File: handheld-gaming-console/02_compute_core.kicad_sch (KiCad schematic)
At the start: 33 parts, among them J3 CM4_MAIN, J4 CM4_PERIPH, J8 Micro_SD_Card, Q3 Q_PMOS_GSD, Q4 Q_NMOS_GSD, SW1 SW_SPDT, SW2 SW_Push, U5 TS3USB221A

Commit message: feat(display): implement AP3031 38V constant-current WLED backlight boost driver with PWM dimming and aux header
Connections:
- net LCD_BL_PWM: now reaches J3.54 (Pin_54)
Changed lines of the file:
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@@
+	(wire
+		(pts
+			(xy 87.63 104.14) (xy 88.9 104.14)
+		)
+		(stroke
+			(width 0)
+			(type default)
+		)
+	)
 	(wire
 		(pts
@@
 			)
 		)
+	)
+	(global_label "LCD_BL_PWM"
+		(shape input)
+		(at 88.9 104.14 0)
+		(fields_autoplaced yes)
+		(effects
+			(font
+				(size 1.27 1.27)
+			)
+			(justify left)
+		)
+		(property "Intersheetrefs" "${INTERSHEET_REFS}"
+			(at 103.8594 104.14 0)
+			(hide yes)
+			(show_name no)
+			(do_not_autoplace no)
+			(effects
+				(font
+					(size 1.27 1.27)
+				)
+				(justify left)
+			)
+		)

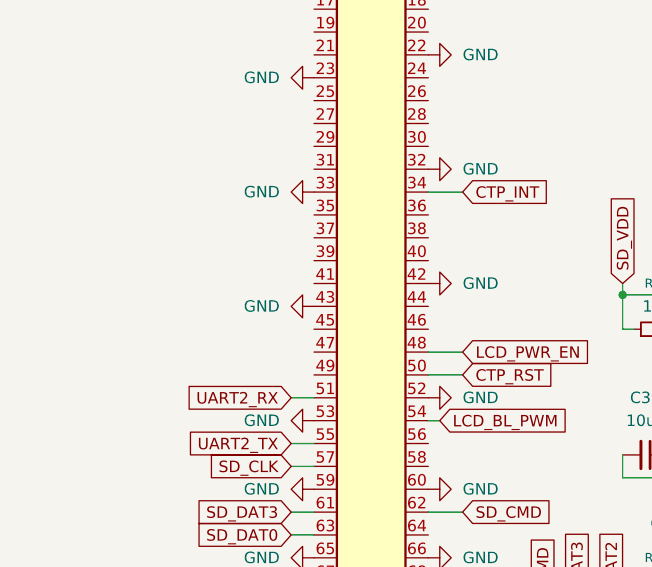
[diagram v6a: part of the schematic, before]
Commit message: feat(audio): tap I2S bus from Core3566 and implement isolated MAX98357A Class-D speaker amplifier
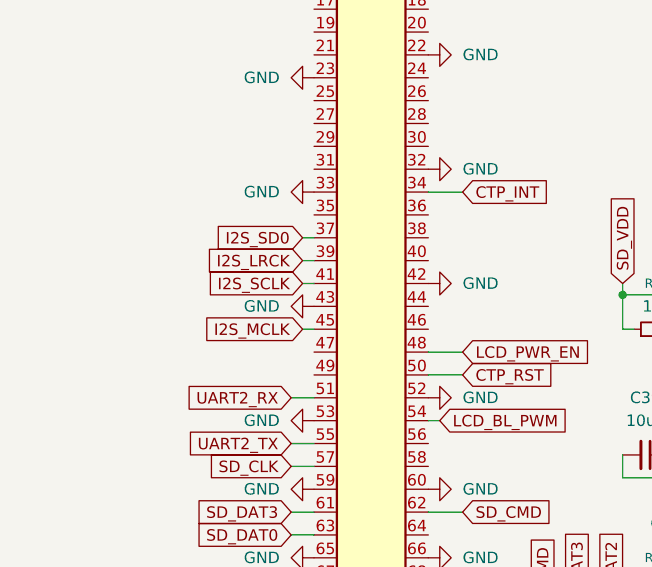
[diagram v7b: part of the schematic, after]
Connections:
- net I2S_SD0: now reaches J3.37 (Pin_37)
- net I2S_LRCK: now reaches J3.39 (Pin_39)
- net I2S_SCLK: now reaches J3.41 (Pin_41)
- net I2S_MCLK: now reaches J3.45 (Pin_45)
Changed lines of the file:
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@@
+	(wire
+		(pts
+			(xy 73.66 86.36) (xy 74.93 86.36)
+		)
+		(stroke
+			(width 0)
+			(type default)
+		)
+	)
 	(wire
 		(pts
@@
 	(wire
 		(pts
+			(xy 73.66 83.82) (xy 74.93 83.82)
+		)
+		(stroke
+			(width 0)
+			(type default)
+		)
+	)
+	(wire
+		(pts
 			(xy 223.52 55.88) (xy 251.46 55.88)
 		)
@@
 	(wire
 		(pts
+			(xy 73.66 93.98) (xy 74.93 93.98)
+		)
+		(stroke
+			(width 0)
+			(type default)
+		)
+	)
+	(wire
+		(pts
 			(xy 120.65 90.17) (xy 118.11 90.17)
 		)
@@
 	(wire
 		(pts
+			(xy 73.66 88.9) (xy 74.93 88.9)
+		)
+		(stroke
+			(width 0)
+			(type default)
+		)
+	)
+	(wire
+		(pts
 			(xy 125.73 119.38) (xy 125.73 107.95)
 		)
@@
 		)
 	)
+	(global_label "I2S_SD0"
+		(shape input)
+		(at 73.66 83.82 180)
+		(fields_autoplaced yes)
+		(effects
+			(font
+				(size 1.27 1.27)
+			)
+			(justify right)
+		)
+		(property "Intersheetrefs" "${INTERSHEET_REFS}"
+			(at 62.9944 83.82 0)
+			(hide yes)
+			(show_name no)
+			(do_not_autoplace no)
+			(effects
+				(font
+					(size 1.27 1.27)
+				)
+				(justify right)
+			)
+		)
+	)
 	(global_label "USB_OTG_ID"
 		(shape input)
@@
 		)
 	)
+	(global_label "I2S_SCLK"
+		(shape input)
+		(at 73.66 88.9 180)
+		(fields_autoplaced yes)
+		(effects
+			(font
+				(size 1.27 1.27)
+			)
+			(justify right)
+		)
+		(property "Intersheetrefs" "${INTERSHEET_REFS}"
+			(at 61.9058 88.9 0)
+			(hide yes)
+			(show_name no)
+			(do_not_autoplace no)
+			(effects
+				(font
+					(size 1.27 1.27)
+				)
+				(justify right)
+			)
+		)
+	)
 	(global_label "CTP_INT"
 		(shape input)
@@
 		)
 	)
+	(global_label "I2S_MCLK"
+		(shape input)
+		(at 73.66 93.98 180)
+		(fields_autoplaced yes)
+		(effects
+			(font
+				(size 1.27 1.27)
+			)
+			(justify right)
+		)
+		(property "Intersheetrefs" "${INTERSHEET_REFS}"
+			(at 61.6639 93.98 0)
+			(hide yes)
+			(show_name no)
+			(do_not_autoplace no)
+			(effects
+				(font
+					(size 1.27 1.27)
+				)
+				(justify right)
+			)
+		)
+	)
 	(global_label "LCD_PWR_EN"
 		(shape input)
@@
 			(hide yes)
 			(show_name no)
+			(do_not_autoplace no)
+			(effects
+				(font
+					(size 1.27 1.27)
+				)
+				(justify right)
+			)
+		)
+	)
+	(global_label "I2S_LRCK"
+		(shape input)
+		(at 73.66 86.36 180)
+		(fields_autoplaced yes)
+		(effects
+			(font
+				(size 1.27 1.27)
+			)
+			(justify right)
+		)
+		(property "Intersheetrefs" "${INTERSHEET_REFS}"
+			(at 61.8453 86.36 0)
+			(hide yes)
+			(show_name no)
